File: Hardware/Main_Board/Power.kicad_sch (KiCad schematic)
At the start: 0 parts

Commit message: Added buck converter datasheet, and symbols to project
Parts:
- added U2: LM2596DSADJG, ESP32-footprints:CONV_LM2596DSADJG, symbol ESP32-Symbols:LM2596DSADJG
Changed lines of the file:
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@@
 	(generator_version "9.0")
 	(paper "A4")
+	(symbol
+		(lib_id "ESP32-Symbols:LM2596DSADJG")
+		(at 105.41 67.31 0)
+		(unit 1)
+		(exclude_from_sim no)
+		(in_bom yes)
+		(on_board yes)
+		(dnp no)
+		(fields_autoplaced yes)
+		(property "Reference" "U2"
+			(at 105.41 54.61 0)
+			(effects
+				(font
+					(size 1.27 1.27)
+				)
+			)
+		)
+		(property "Value" "LM2596DSADJG"
+			(at 105.41 57.15 0)
+			(effects
+				(font
+					(size 1.27 1.27)
+				)
+			)
+		)
+		(property "Footprint" "ESP32-footprints:CONV_LM2596DSADJG"
+			(at 105.41 67.31 0)
+			(effects
+				(font
+					(size 1.27 1.27)
+				)
+				(justify bottom)
+				(hide yes)
+			)
+		)
+		(property "Datasheet" ""
+			(at 105.41 67.31 0)
+			(effects
+				(font
+					(size 1.27 1.27)
+				)
+				(hide yes)
+			)
+		)
+		(property "Description" ""
+			(at 105.41 67.31 0)
+			(effects
+				(font
+					(size 1.27 1.27)
+				)
+				(hide yes)
+			)
+		)
+		(property "MF" "ON Semiconductor"
+			(at 105.41 67.31 0)
+			(effects
+				(font
+					(size 1.27 1.27)
+				)
+				(justify bottom)
+				(hide yes)
+			)
+		)
+		(property "MAXIMUM_PACKAGE_HEIGHT" "4.572mm"
+			(at 105.41 67.31 0)
+			(effects
+				(font
+					(size 1.27 1.27)
+				)
+				(justify bottom)
+				(hide yes)
+			)
+		)
+		(property "Package" "D2PAK-5 ON Semiconductor"
+			(at 105.41 67.31 0)
+			(effects
+				(font
+					(size 1.27 1.27)
+				)
+				(justify bottom)
+				(hide yes)
+			)
+		)
+		(property "Price" "None"
+			(at 105.41 67.31 0)
+			(effects
+				(font
+					(size 1.27 1.27)
+				)
+				(justify bottom)
+				(hide yes)
+			)
+		)
+		(property "Check_prices" "https://www.snapeda.com/parts/LM2596DSADJG/Onsemi/view-part/?ref=eda"
+			(at 105.41 67.31 0)
+			(effects
+				(font
+					(size 1.27 1.27)
+				)
+				(justify bottom)
+				(hide yes)
+			)
+		)
+		(property "STANDARD" "Manufacturer recommendations"
+			(at 105.41 67.31 0)
+			(effects
+				(font
+					(size 1.27 1.27)
+				)
+				(justify bottom)
+				(hide yes)
+			)
+		)
+		(property "PARTREV" "0"
+			(at 105.41 67.31 0)
+			(effects
+				(font
+					(size 1.27 1.27)
+				)
+				(justify bottom)
+				(hide yes)
+			)
+		)
+		(property "SnapEDA_Link" "https://www.snapeda.com/parts/LM2596DSADJG/Onsemi/view-part/?ref=snap"
+			(at 105.41 67.31 0)
+			(effects
+				(font
+					(size 1.27 1.27)
+				)
+				(justify bottom)
+				(hide yes)
+			)
+		)
+		(property "MP" "LM2596DSADJG"
+			(at 105.41 67.31 0)
+			(effects
+				(font
+					(size 1.27 1.27)
+				)
+				(justify bottom)
+				(hide yes)
+			)
+		)
+		(property "Description_1" "LM2596DSADJG Switching Regulator 3A Adjustable, 1.23 to 37 V, 5-Pin D2PAK | ON Semiconductor LM2596DSADJG"
+			(at 105.41 67.31 0)
+			(effects
+				(font
+					(size 1.27 1.27)
+				)
+				(justify bottom)
+				(hide yes)
+			)
+		)
+		(property "Availability" "In Stock"
+			(at 105.41 67.31 0)
+			(effects
+				(font
+					(size 1.27 1.27)
+				)
+				(justify bottom)
+				(hide yes)
+			)
+		)
+		(property "MANUFACTURER" "On Semiconductor"
+			(at 105.41 67.31 0)
+			(effects
+				(font
+					(size 1.27 1.27)
+				)
+				(justify bottom)
+				(hide yes)
+			)
+		)
+		(pin "2"
+		)
+		(pin "5"
+		)
+		(pin "1"
+		)
+		(pin "4"
+		)
+		(pin "3"
+		)
+		(pin "6"
+		)
+		(instances
+			(project ""
+				(path "/3bfaeaa6-4337-4b5f-9f42-0e28df6ecb69/88b7e6bf-fd05-40a1-af72-862ac58f0449"
+					(reference "U2")
+					(unit 1)
+				)
+			)
+		)
+	)
 )

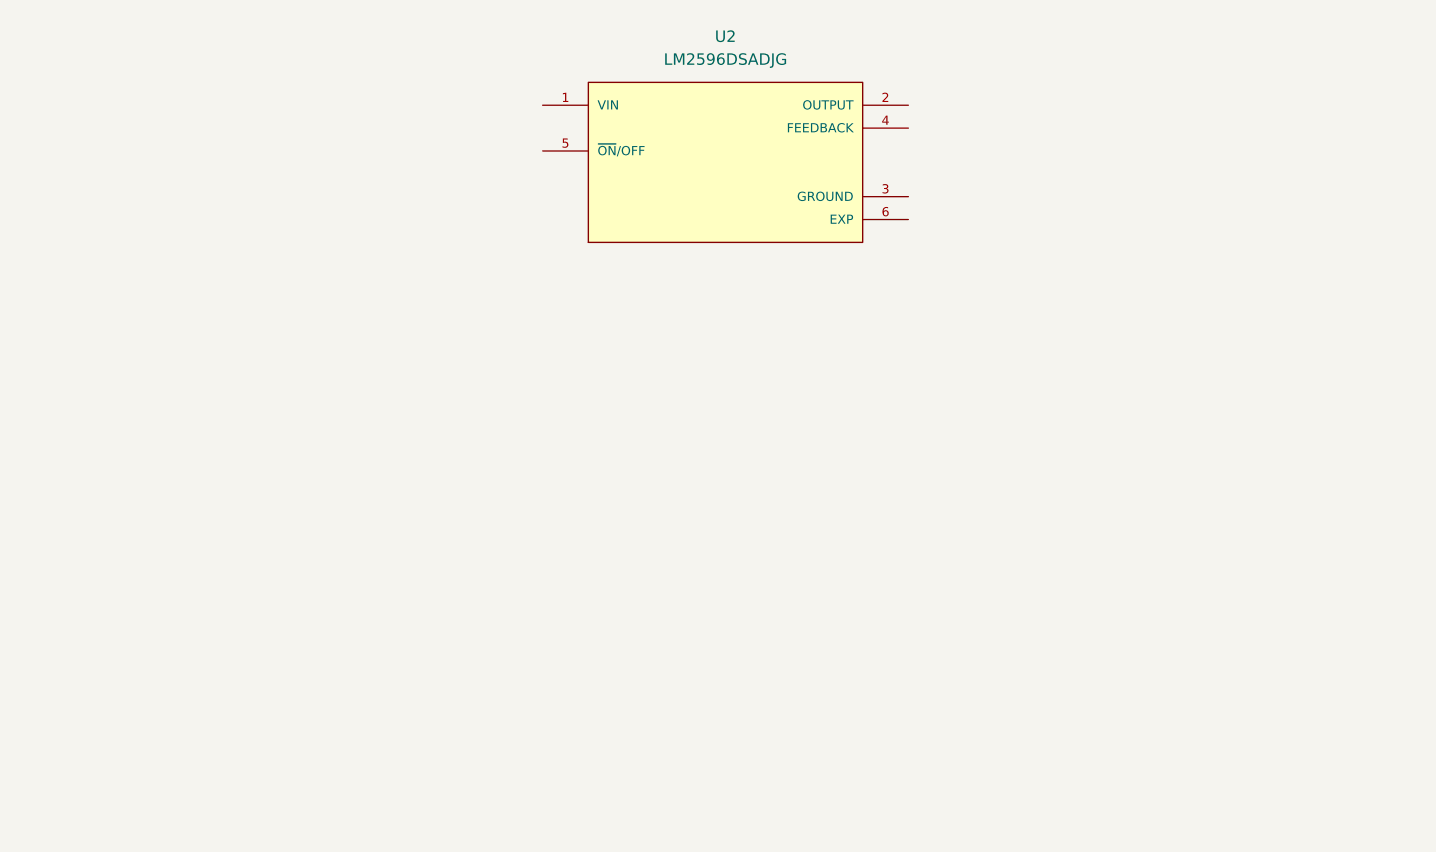
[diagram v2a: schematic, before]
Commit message: finished most of the main board
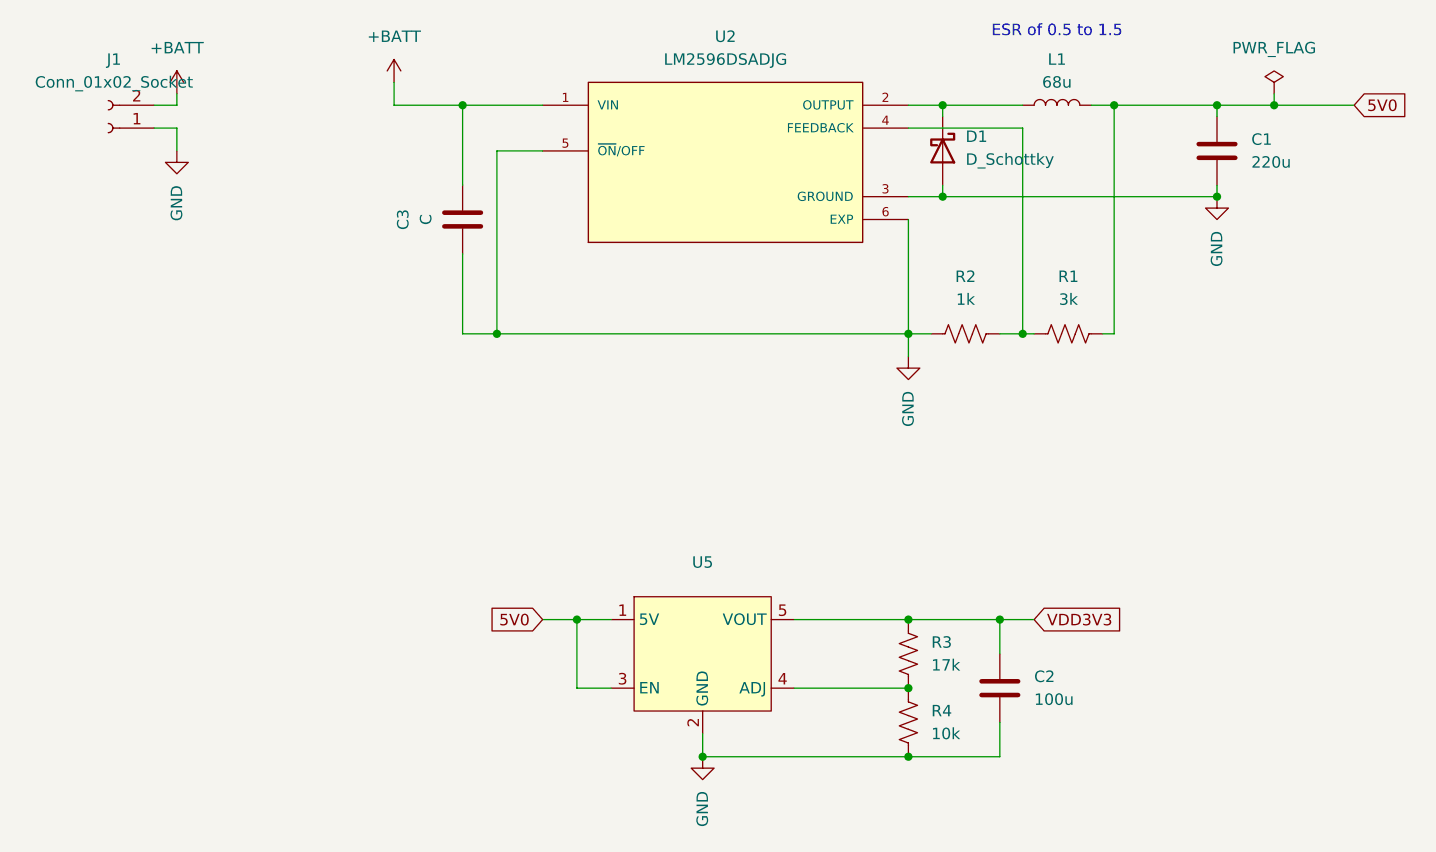
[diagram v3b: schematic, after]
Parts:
- added C1: 220u, Capacitor_THT:CP_Radial_D4.0mm_P1.50mm, symbol Device:C
- added C2: 100u, Capacitor_SMD:C_0805_2012Metric, symbol Device:C
- added C3: C, Capacitor_SMD:C_0805_2012Metric, symbol Device:C
- added D1: D_Schottky, Capacitor_SMD:C_0805_2012Metric, symbol Device:D_Schottky
- added J1: Conn_01x02_Socket, TerminalBlock:TerminalBlock_bornier-2_P5.08mm, symbol Connector:Conn_01x02_Socket
- added L1: 68u, Inductor_SMD:L_0603_1608Metric, symbol Device:L
- added R1: 3k, Resistor_SMD:R_0603_1608Metric, symbol Device:R_US
- added R2: 1k, Resistor_SMD:R_0603_1608Metric, symbol Device:R_US
- added R3: 17k, Resistor_SMD:R_0603_1608Metric, symbol Device:R_US
- added R4: 10k, Resistor_SMD:R_0603_1608Metric, symbol Device:R_US
- added U5: ~, Package_TO_SOT_SMD:SOT-23-5, symbol ESP32-Symbols:SPX5205-ADJ
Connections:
- net +BATT: now reaches U2.1 (VIN)
- net +BATT: now also C3.2, J1.2 (Pin_2)
- net at U2.2 (OUTPUT): now also D1.1 (K), L1.1
- net GND: now reaches U2.3 (GROUND)
- net GND: now also U2.5 (~{ON}/OFF), U2.6 (EXP), C1.2, C2.2, C3.1, D1.2 (A), J1.1 (Pin_1), R2.1, R4.1, U5.2 (GND)
- net at U2.4 (FEEDBACK): now also R1.1, R2.2
- new net: R3.1, R4.2, U5.4 (ADJ)
- new net 5V0: C1.1, L1.2, R1.2, U5.1 (5V), U5.3 (EN)
- new net VDD3V3: C2.1, R3.2, U5.5 (VOUT)
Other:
- note added: "ESR of 0.5 to 1.5"

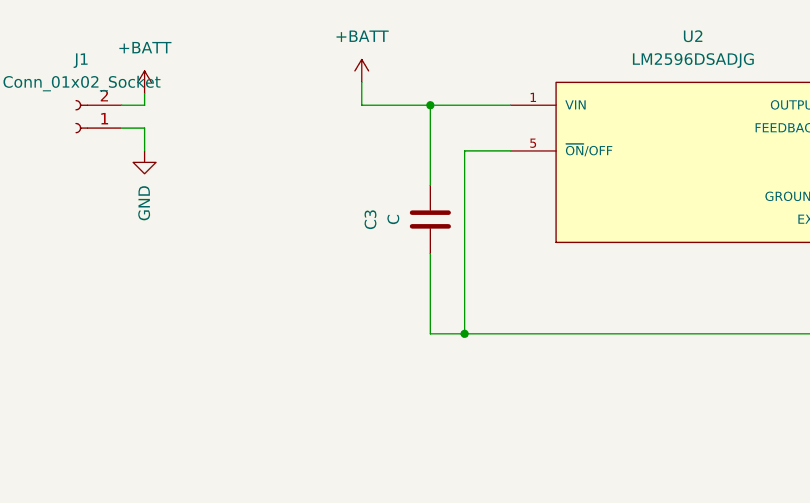
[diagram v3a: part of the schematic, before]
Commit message: added gerbers, drill files, BOM and CPL for the main board
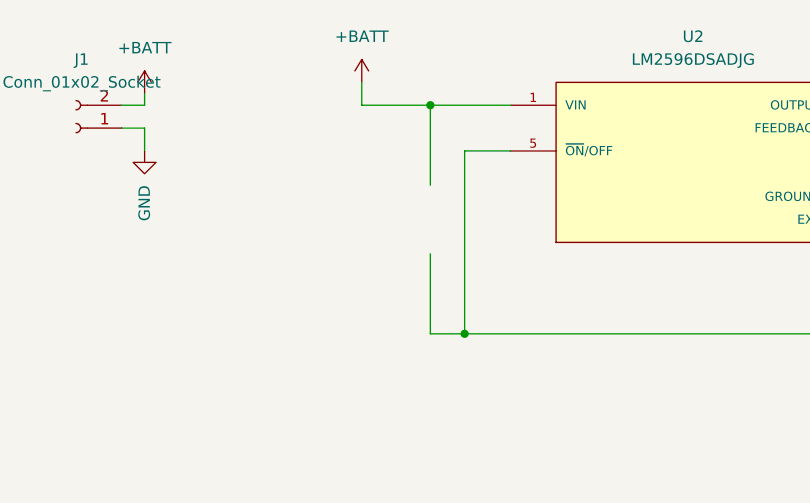
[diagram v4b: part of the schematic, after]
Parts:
- removed C3: C, Capacitor_SMD:C_0805_2012Metric, symbol Device:C
- L1: footprint Inductor_SMD:L_0603_1608Metric -> Inductor_SMD:L_0805_2012Metric
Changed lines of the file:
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@@
 			)
 		)
-		(property "Footprint" "Inductor_SMD:L_0603_1608Metric"
+		(property "Footprint" "Inductor_SMD:L_0805_2012Metric"
 			(at 142.24 62.23 0)
 			(effects
@@
 					(unit 1)
 				)
-			)
-		)
-	)
-	(symbol
-		(lib_id "Device:C")
-		(at 76.2 74.93 180)
-		(unit 1)
-		(exclude_from_sim no)
-		(in_bom yes)
-		(on_board yes)
-		(dnp no)
-		(property "Reference" "C3"
-			(at 69.596 74.93 90)
-			(effects
-				(font
-					(size 1.27 1.27)
-				)
-			)
-		)
-		(property "Value" "C"
-			(at 72.136 74.93 90)
-			(effects
-				(font
-					(size 1.27 1.27)
-				)
-			)
-		)
-		(property "Footprint" "Capacitor_SMD:C_0805_2012Metric"
-			(at 75.2348 71.12 0)
-			(effects
-				(font
-					(size 1.27 1.27)
-				)
-				(hide yes)
-			)
-		)
-		(property "Datasheet" "~"
-			(at 76.2 74.93 0)
-			(effects
-				(font
-					(size 1.27 1.27)
-				)
-				(hide yes)
-			)
-		)
-		(property "Description" "Unpolarized capacitor"
-			(at 76.2 74.93 0)
-			(effects
-				(font
-					(size 1.27 1.27)
-				)
-				(hide yes)
-			)
-		)
-		(pin "1"
-		)
-		(pin "2"
-		)
-		(instances
-			(project "Main_Board"
-				(path "/3bfaeaa6-4337-4b5f-9f42-0e28df6ecb69/88b7e6bf-fd05-40a1-af72-862ac58f0449"
-					(reference "C3")
-					(unit 1)
-				)
